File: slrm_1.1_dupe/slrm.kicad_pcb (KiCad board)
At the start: 4 copper layers, 82.1 x 22.5 mm, 26 parts, among them J1 Conn_01x08_Male, J8 Conn_01x08_Male

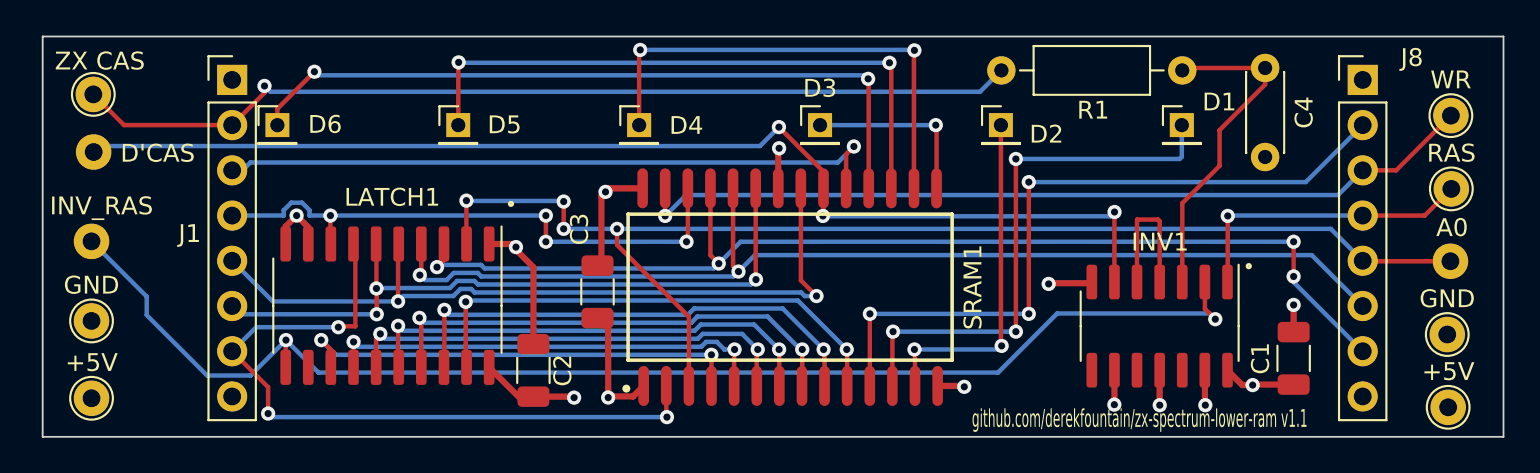
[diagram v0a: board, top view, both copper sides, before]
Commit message: v1.1, added RC circuit to main design, added a breakout version (debug) and a duplication of a working circuit
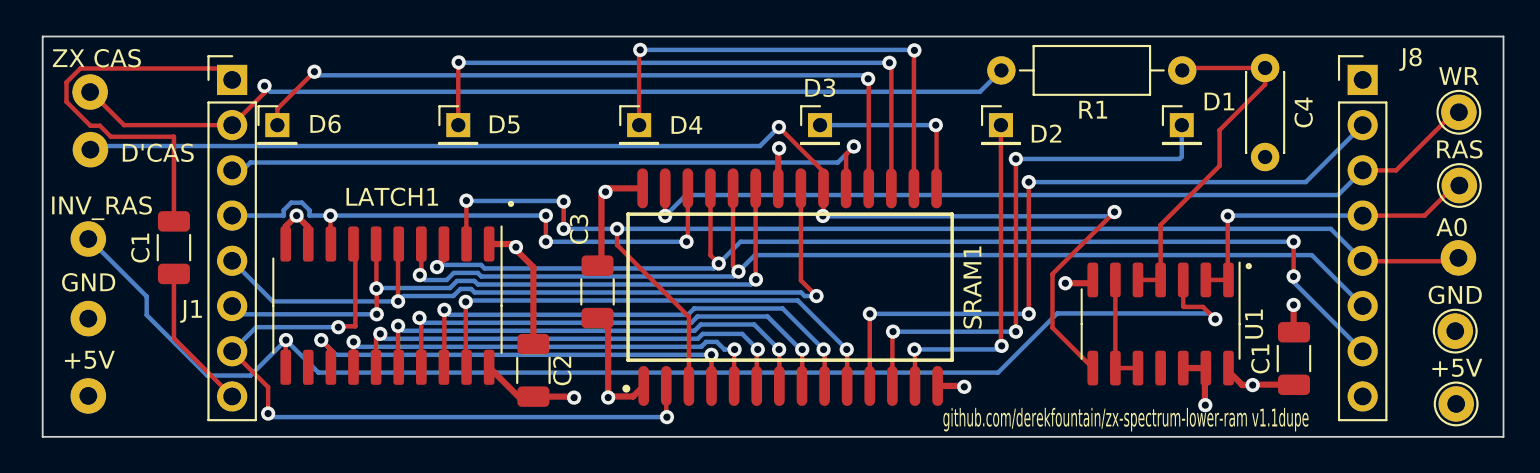
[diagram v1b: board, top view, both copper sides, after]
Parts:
- removed the +5V at (111.5, 104.2)
- removed the +5V at (187.7, 104.7)
- removed the ? at (111.5, 95.4)
- removed the ? at (187.8, 96.5)
- removed the ? at (111.6, 90.4)
- removed the C1 at (179.0, 102.0)
- removed the GND at (187.6, 100.7)
- removed the GND at (111.5, 99.9)
- removed INV1: 74HCT04, Package_SO:SOIC-14_3.9x8.7mm_P1.27mm
- removed ZX CAS: TestPoint_THTPad_D2.0mm_Drill1.0mm, TestPoint:TestPoint_THTPad_D2.0mm_Drill1.0mm
- added +5V: TestPoint_THTPad_D2.0mm_Drill1.0mm, TestPoint:TestPoint_THTPad_D2.0mm_Drill1.0mm, F.Cu at (188.1, 104.6)
- added ?: , , F.Cu at (188.3, 96.4)
- added ?: , , F.Cu at (111.3, 104.1)
- added ?: , , F.Cu at (111.4, 90.3)
- added ?: , , F.Cu at (111.4, 87.0)
- added ?: , , F.Cu at (111.3, 95.3)
- added ?: , , F.Cu at (111.3, 99.8)
- added C1: C_Small, Capacitor_SMD:C_1206_3216Metric, F.Cu at (116.1, 95.8)
- added C1: C_Small, Capacitor_SMD:C_1206_3216Metric, F.Cu at (179.0, 102.0)
- added GND: TestPoint_THTPad_D2.0mm_Drill1.0mm, TestPoint:TestPoint_THTPad_D2.0mm_Drill1.0mm, F.Cu at (188.1, 100.5)
- added U1: 74HCT00, Package_SO:SOIC-14_3.9x8.7mm_P1.27mm, F.Cu at (171.5, 100.1)
- moved RAS 0.49 mm to (188.3, 92.3)
- moved WR 0.49 mm to (188.3, 88.2)
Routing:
- net GND: track 31.8 -> 50.8 mm, vias 10 -> 8
- net +5V: track 16.0 -> 24.2 mm
- net DELAYED_CAS: track 66.4 -> 73.6 mm
- net INV_DELAYED_ZX_CAS: track 8.24 -> 6.22 mm
- net DELAYED_ZX_CAS: track 18.7 -> 20.3 mm
- net ZX_RAS: track 16.9 -> 18.2 mm
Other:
- board text added: "+5V"
- board text added: "GND"
- board text added: "ZX CAS"
- board text added: "github.com/derekfountain/zx-spectrum-lower-ram v1.1dupe"
- board text removed: "github.com/derekfountain/zx-spectrum-lower-ram v1.1"
